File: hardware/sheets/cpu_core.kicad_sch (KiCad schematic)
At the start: 32 parts, among them U1 V20, U10 74HCT32, U11 74HCT125, U12 74HCT157, U13 74HCT04, U14 TCM809, U2 74HCT573, U3 74HCT573, U4 74HCT573, U5 74HCT245, U6 74HCT138, U7 74HCT00, U8 74HCT74, U9 74HCT163

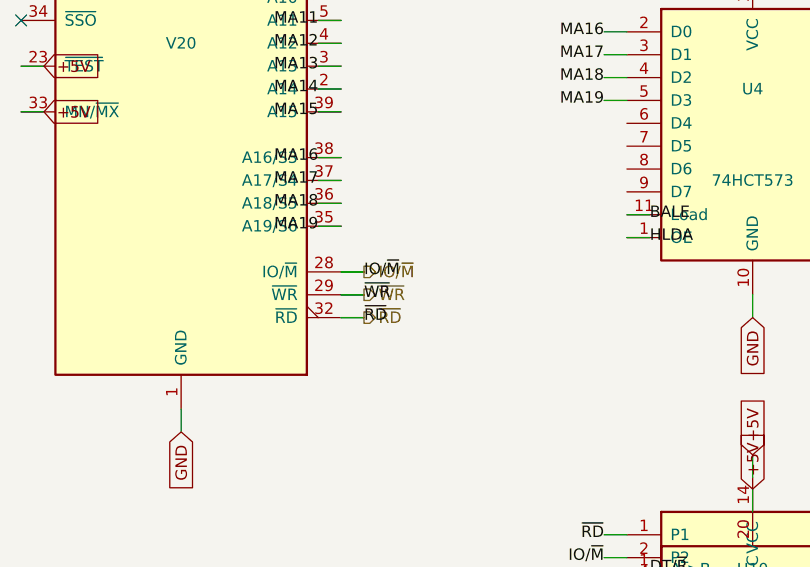
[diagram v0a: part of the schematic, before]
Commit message: Fix all medium design-review findings (M1-M8)
- M1: Supervisor link moved to GPIO4/5 (real UART1 pair); POST -> GPIO6-15
- M2: CNT_RUN = LD0.LD1.LD2 gates every '163 CEP (load-cascade hazard)
- M3: ~WR / IO-M pruned to cpu_core-internal; DRQ2/3 pulled + noted;
  doc S5.2 "as built: 48/48" + S16 updated
- M4: true XT-IDE rev-2 map (A0<->A3 swap): data 0x300, latch 0x301,
  CS1 0x307/0x30F, drive DA0 = bus A3 - matches XTIDE UB "rev 2" type
- M5: COM4 -> bus IRQ2 line (IRQ9 via AT redirect); IRQ10/11/14/15 marked
  off-header; ~REFRESH added to mxbus ISA_CTRL; questions-sidecar superseded
- M6: card_isatest clock tree on unswitched V5RAW (spec S8)
- M7: card_isatest IRQ2-8/DRQ1-3 idle pull-downs (spec S4/S9)
- M8: com_port JP1 selects 16550 RX source (DB9 vs TTL console); 5V note

Rebuilt motherboard + cards; structural ERC = 0; netlist-verified.
Fix log in hardware/notes/design-review-2026-07-03.md (batch 3).

Co-Authored-By: Claude Fable 5 <noreply@anthropic.com>
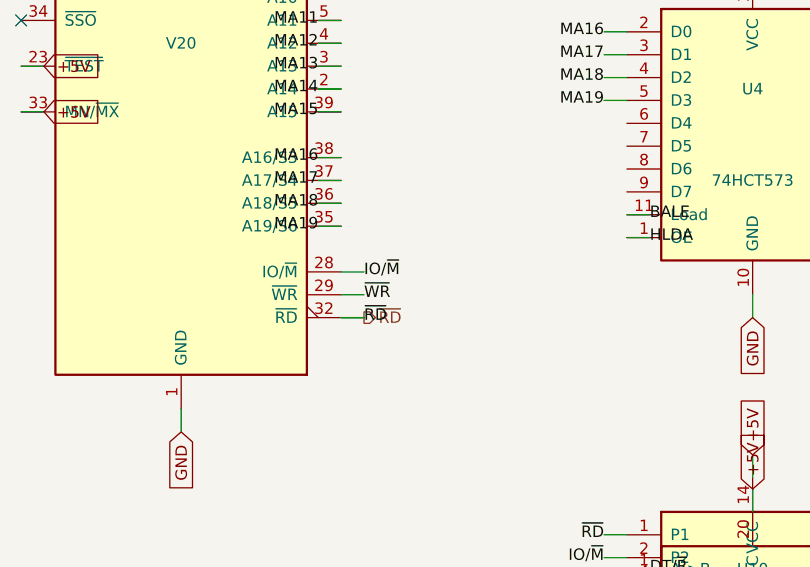
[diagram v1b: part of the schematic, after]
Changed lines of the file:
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@@
 	(wire
 		(pts
-			(xy 119.38 185.42)
-			(xy 121.92 185.42)
-		)
-		(stroke
-			(width 0)
-			(type default)
-		)
-	)
-	(hierarchical_label "~{WR}"
-		(shape output)
-		(at 121.92 185.42 0)
-		(effects
-			(font
-				(size 1.27 1.27)
-			)
-		)
-	)
-	(wire
-		(pts
-			(xy 119.38 182.88)
-			(xy 121.92 182.88)
-		)
-		(stroke
-			(width 0)
-			(type default)
-		)
-	)
-	(hierarchical_label "IO/~{M}"
-		(shape output)
-		(at 121.92 182.88 0)
-		(effects
-			(font
-				(size 1.27 1.27)
-			)
-		)
-	)
-	(wire
-		(pts
 			(xy 165.1 205.74)
 			(xy 165.1 203.2)
@@
 		(instances
 			(project "mini-xt"
-				(path "/ccbe75bb-9744-49b2-888c-84927206f4cb/9efb1572-68dd-4ca6-96f4-928422b9a1fb"
+				(path "/9d1a32b9-fdc3-4ebf-878d-e57919a1b88e/ead79a1c-d771-4618-8d33-c03035d0f824"
 					(reference "U101")
 					(unit 1)
@@
 		(instances
 			(project "mini-xt"
-				(path "/ccbe75bb-9744-49b2-888c-84927206f4cb/9efb1572-68dd-4ca6-96f4-928422b9a1fb"
+				(path "/9d1a32b9-fdc3-4ebf-878d-e57919a1b88e/ead79a1c-d771-4618-8d33-c03035d0f824"
 					(reference "U110")
 					(unit 1)
@@
 		(instances
 			(project "mini-xt"
-				(path "/ccbe75bb-9744-49b2-888c-84927206f4cb/9efb1572-68dd-4ca6-96f4-928422b9a1fb"
+				(path "/9d1a32b9-fdc3-4ebf-878d-e57919a1b88e/ead79a1c-d771-4618-8d33-c03035d0f824"
 					(reference "U111")
 					(unit 1)
@@
 		(instances
 			(project "mini-xt"
-				(path "/ccbe75bb-9744-49b2-888c-84927206f4cb/9efb1572-68dd-4ca6-96f4-928422b9a1fb"
+				(path "/9d1a32b9-fdc3-4ebf-878d-e57919a1b88e/ead79a1c-d771-4618-8d33-c03035d0f824"
 					(reference "U102")
 					(unit 1)
@@
 		(instances
 			(project "mini-xt"
-				(path "/ccbe75bb-9744-49b2-888c-84927206f4cb/9efb1572-68dd-4ca6-96f4-928422b9a1fb"
+				(path "/9d1a32b9-fdc3-4ebf-878d-e57919a1b88e/ead79a1c-d771-4618-8d33-c03035d0f824"
 					(reference "U103")
 					(unit 1)
@@
 		(instances
 			(project "mini-xt"
-				(path "/ccbe75bb-9744-49b2-888c-84927206f4cb/9efb1572-68dd-4ca6-96f4-928422b9a1fb"
+				(path "/9d1a32b9-fdc3-4ebf-878d-e57919a1b88e/ead79a1c-d771-4618-8d33-c03035d0f824"
 					(reference "U104")
 					(unit 1)
@@
 		(instances
 			(project "mini-xt"
-				(path "/ccbe75bb-9744-49b2-888c-84927206f4cb/9efb1572-68dd-4ca6-96f4-928422b9a1fb"
+				(path "/9d1a32b9-fdc3-4ebf-878d-e57919a1b88e/ead79a1c-d771-4618-8d33-c03035d0f824"
 					(reference "U105")
 					(unit 1)
@@
 		(instances
 			(project "mini-xt"
-				(path "/ccbe75bb-9744-49b2-888c-84927206f4cb/9efb1572-68dd-4ca6-96f4-928422b9a1fb"
+				(path "/9d1a32b9-fdc3-4ebf-878d-e57919a1b88e/ead79a1c-d771-4618-8d33-c03035d0f824"
 					(reference "U106")
 					(unit 1)
@@
 		(instances
 			(project "mini-xt"
-				(path "/ccbe75bb-9744-49b2-888c-84927206f4cb/9efb1572-68dd-4ca6-96f4-928422b9a1fb"
+				(path "/9d1a32b9-fdc3-4ebf-878d-e57919a1b88e/ead79a1c-d771-4618-8d33-c03035d0f824"
 					(reference "U107")
 					(unit 1)
@@
 		(instances
 			(project "mini-xt"
-				(path "/ccbe75bb-9744-49b2-888c-84927206f4cb/9efb1572-68dd-4ca6-96f4-928422b9a1fb"
+				(path "/9d1a32b9-fdc3-4ebf-878d-e57919a1b88e/ead79a1c-d771-4618-8d33-c03035d0f824"
 					(reference "RAM101")
 					(unit 1)
@@
 		(instances
 			(project "mini-xt"
-				(path "/ccbe75bb-9744-49b2-888c-84927206f4cb/9efb1572-68dd-4ca6-96f4-928422b9a1fb"
+				(path "/9d1a32b9-fdc3-4ebf-878d-e57919a1b88e/ead79a1c-d771-4618-8d33-c03035d0f824"
 					(reference "RAM102")
 					(unit 1)
@@
 		(instances
 			(project "mini-xt"
-				(path "/ccbe75bb-9744-49b2-888c-84927206f4cb/9efb1572-68dd-4ca6-96f4-928422b9a1fb"
+				(path "/9d1a32b9-fdc3-4ebf-878d-e57919a1b88e/ead79a1c-d771-4618-8d33-c03035d0f824"
 					(reference "OSC101")
 					(unit 1)
@@
 		(instances
 			(project "mini-xt"
-				(path "/ccbe75bb-9744-49b2-888c-84927206f4cb/9efb1572-68dd-4ca6-96f4-928422b9a1fb"
+				(path "/9d1a32b9-fdc3-4ebf-878d-e57919a1b88e/ead79a1c-d771-4618-8d33-c03035d0f824"
 					(reference "U108")
 					(unit 1)
@@
 		(instances
 			(project "mini-xt"
-				(path "/ccbe75bb-9744-49b2-888c-84927206f4cb/9efb1572-68dd-4ca6-96f4-928422b9a1fb"
+				(path "/9d1a32b9-fdc3-4ebf-878d-e57919a1b88e/ead79a1c-d771-4618-8d33-c03035d0f824"
 					(reference "U109")
 					(unit 1)
@@
 		(instances
 			(project "mini-xt"
-				(path "/ccbe75bb-9744-49b2-888c-84927206f4cb/9efb1572-68dd-4ca6-96f4-928422b9a1fb"
+				(path "/9d1a32b9-fdc3-4ebf-878d-e57919a1b88e/ead79a1c-d771-4618-8d33-c03035d0f824"
 					(reference "U112")
 					(unit 1)
@@
 		(instances
 			(project "mini-xt"
-				(path "/ccbe75bb-9744-49b2-888c-84927206f4cb/9efb1572-68dd-4ca6-96f4-928422b9a1fb"
+				(path "/9d1a32b9-fdc3-4ebf-878d-e57919a1b88e/ead79a1c-d771-4618-8d33-c03035d0f824"
 					(reference "U113")
 					(unit 1)
@@
 		(instances
 			(project "mini-xt"
-				(path "/ccbe75bb-9744-49b2-888c-84927206f4cb/9efb1572-68dd-4ca6-96f4-928422b9a1fb"
+				(path "/9d1a32b9-fdc3-4ebf-878d-e57919a1b88e/ead79a1c-d771-4618-8d33-c03035d0f824"
 					(reference "U114")
 					(unit 1)
@@
 		(instances
 			(project "mini-xt"
-				(path "/ccbe75bb-9744-49b2-888c-84927206f4cb/9efb1572-68dd-4ca6-96f4-928422b9a1fb"
+				(path "/9d1a32b9-fdc3-4ebf-878d-e57919a1b88e/ead79a1c-d771-4618-8d33-c03035d0f824"
 					(reference "R101")
 					(unit 1)
@@
 		(instances
 			(project "mini-xt"
-				(path "/ccbe75bb-9744-49b2-888c-84927206f4cb/9efb1572-68dd-4ca6-96f4-928422b9a1fb"
+				(path "/9d1a32b9-fdc3-4ebf-878d-e57919a1b88e/ead79a1c-d771-4618-8d33-c03035d0f824"
 					(reference "R102")
 					(unit 1)
@@
 		(instances
 			(project "mini-xt"
-				(path "/ccbe75bb-9744-49b2-888c-84927206f4cb/9efb1572-68dd-4ca6-96f4-928422b9a1fb"
+				(path "/9d1a32b9-fdc3-4ebf-878d-e57919a1b88e/ead79a1c-d771-4618-8d33-c03035d0f824"
 					(reference "R103")
 					(unit 1)
@@
 		(instances
 			(project "mini-xt"
-				(path "/ccbe75bb-9744-49b2-888c-84927206f4cb/9efb1572-68dd-4ca6-96f4-928422b9a1fb"
+				(path "/9d1a32b9-fdc3-4ebf-878d-e57919a1b88e/ead79a1c-d771-4618-8d33-c03035d0f824"
 					(reference "R104")
 					(unit 1)
@@
 		(instances
 			(project "mini-xt"
-				(path "/ccbe75bb-9744-49b2-888c-84927206f4cb/9efb1572-68dd-4ca6-96f4-928422b9a1fb"
+				(path "/9d1a32b9-fdc3-4ebf-878d-e57919a1b88e/ead79a1c-d771-4618-8d33-c03035d0f824"
 					(reference "R105")
 					(unit 1)
@@
 		(instances
 			(project "mini-xt"
-				(path "/ccbe75bb-9744-49b2-888c-84927206f4cb/9efb1572-68dd-4ca6-96f4-928422b9a1fb"
+				(path "/9d1a32b9-fdc3-4ebf-878d-e57919a1b88e/ead79a1c-d771-4618-8d33-c03035d0f824"
 					(reference "R106")
 					(unit 1)
@@
 		(instances
 			(project "mini-xt"
-				(path "/ccbe75bb-9744-49b2-888c-84927206f4cb/9efb1572-68dd-4ca6-96f4-928422b9a1fb"
+				(path "/9d1a32b9-fdc3-4ebf-878d-e57919a1b88e/ead79a1c-d771-4618-8d33-c03035d0f824"
 					(reference "R107")
 					(unit 1)
@@
 		(instances
 			(project "mini-xt"
-				(path "/ccbe75bb-9744-49b2-888c-84927206f4cb/9efb1572-68dd-4ca6-96f4-928422b9a1fb"
+				(path "/9d1a32b9-fdc3-4ebf-878d-e57919a1b88e/ead79a1c-d771-4618-8d33-c03035d0f824"
 					(reference "R108")
 					(unit 1)
@@
 		(instances
 			(project "mini-xt"
-				(path "/ccbe75bb-9744-49b2-888c-84927206f4cb/9efb1572-68dd-4ca6-96f4-928422b9a1fb"
+				(path "/9d1a32b9-fdc3-4ebf-878d-e57919a1b88e/ead79a1c-d771-4618-8d33-c03035d0f824"
 					(reference "C110")
 					(unit 1)
@@
 		(instances
 			(project "mini-xt"
-				(path "/ccbe75bb-9744-49b2-888c-84927206f4cb/9efb1572-68dd-4ca6-96f4-928422b9a1fb"
+				(path "/9d1a32b9-fdc3-4ebf-878d-e57919a1b88e/ead79a1c-d771-4618-8d33-c03035d0f824"
 					(reference "C111")
 					(unit 1)
@@
 		(instances
 			(project "mini-xt"
-				(path "/ccbe75bb-9744-49b2-888c-84927206f4cb/9efb1572-68dd-4ca6-96f4-928422b9a1fb"
+				(path "/9d1a32b9-fdc3-4ebf-878d-e57919a1b88e/ead79a1c-d771-4618-8d33-c03035d0f824"
 					(reference "C112")
 					(unit 1)
@@
 		(instances
 			(project "mini-xt"
-				(path "/ccbe75bb-9744-49b2-888c-84927206f4cb/9efb1572-68dd-4ca6-96f4-928422b9a1fb"
+				(path "/9d1a32b9-fdc3-4ebf-878d-e57919a1b88e/ead79a1c-d771-4618-8d33-c03035d0f824"
 					(reference "C113")
 					(unit 1)
@@
 		(instances
 			(project "mini-xt"
-				(path "/ccbe75bb-9744-49b2-888c-84927206f4cb/9efb1572-68dd-4ca6-96f4-928422b9a1fb"
+				(path "/9d1a32b9-fdc3-4ebf-878d-e57919a1b88e/ead79a1c-d771-4618-8d33-c03035d0f824"
 					(reference "C114")
 					(unit 1)
@@
 		(instances
 			(project "mini-xt"
-				(path "/ccbe75bb-9744-49b2-888c-84927206f4cb/9efb1572-68dd-4ca6-96f4-928422b9a1fb"
+				(path "/9d1a32b9-fdc3-4ebf-878d-e57919a1b88e/ead79a1c-d771-4618-8d33-c03035d0f824"
 					(reference "C115")
 					(unit 1)
@@
 		(instances
 			(project "mini-xt"
-				(path "/ccbe75bb-9744-49b2-888c-84927206f4cb/9efb1572-68dd-4ca6-96f4-928422b9a1fb"
+				(path "/9d1a32b9-fdc3-4ebf-878d-e57919a1b88e/ead79a1c-d771-4618-8d33-c03035d0f824"
 					(reference "C116")
 					(unit 1)
